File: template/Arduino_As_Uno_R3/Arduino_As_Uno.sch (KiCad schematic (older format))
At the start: 4 parts, among them P1 Power, P2 Analog, P3 Digital, P4 Digital

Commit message: correction holes
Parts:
- added P5, P6, P7, P8: CONN_1, Connect:1pin, symbol CONN_1
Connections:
- no-connect marks 1 -> 5
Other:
- note added: "Holes"
- moved on the sheet: P1, P2, P3, P4

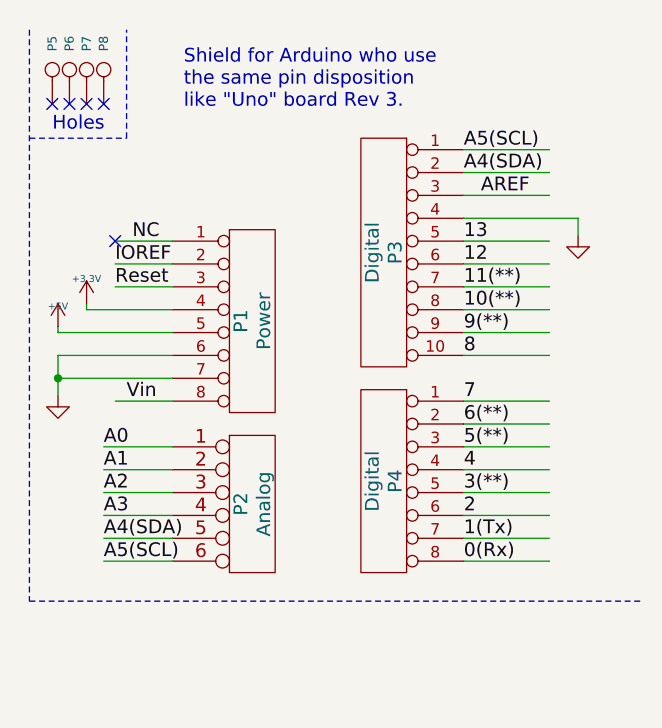
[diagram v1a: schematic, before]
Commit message: correct num holes and add Nano board
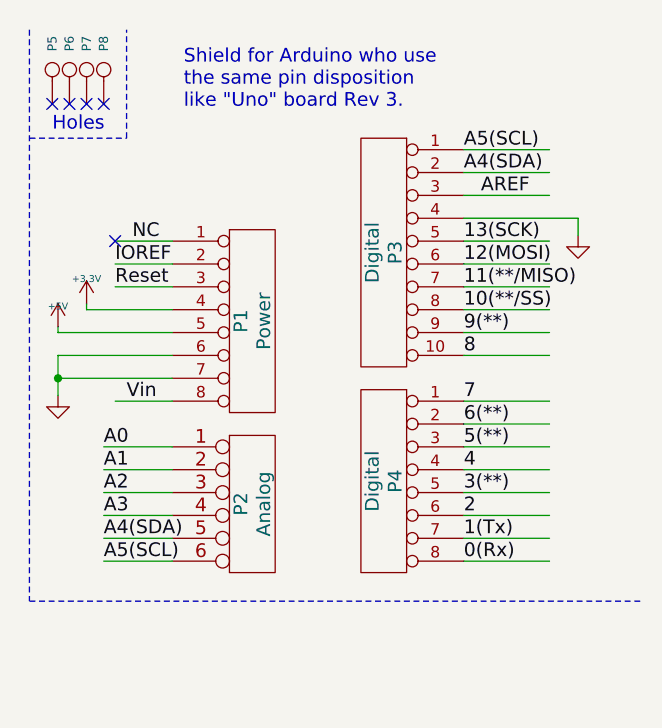
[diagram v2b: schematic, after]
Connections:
- net labels added: 10(**/SS), 11(**/MISO), 12(MOSI), 13(SCK)
- net labels removed: 10(**), 11(**), 12, 13
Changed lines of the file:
@@
 9(**)
 Text Label 10450 1700 0    60   ~ 0
-10(**)
+10(**/SS)
 Text Label 10450 1600 0    60   ~ 0
-11(**)
+11(**/MISO)
 Text Label 10450 1500 0    60   ~ 0
-12
+12(MOSI)
 Text Label 10450 1400 0    60   ~ 0
-13
+13(SCK)
 Text Label 10525 1200 0    60   ~ 0
 AREF

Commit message: Correction schématics
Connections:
- net labels added: 11(**/MOSI), 12(MISO)
- net labels removed: 11(**/MISO), 12(MOSI)
- wire segments 36 -> 38
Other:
- moved on the sheet: P1, P2, P3, P4, P5, P6, P7, P8

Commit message: corrections
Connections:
- net labels removed: NC
- wire segments 38 -> 37
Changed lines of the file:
@@
 	1    0    0    -1
 $EndComp
-NoConn ~ 8600 1525
-Text Label 8625 1525 0    60   ~ 0
-NC
+NoConn ~ 9375 1525
 Text Label 10550 1225 0    60   ~ 0
 A4(SDA)
@@
 	9300 2025 9300 3100
 Wire Wire Line
-	8600 1525 9375 1525
-Wire Wire Line
 	8600 1725 9375 1725

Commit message: add footprint Uno and Mega
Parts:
- P5, P6, P7, P8: footprint Connect:1pin -> Socket_Arduino_Uno:Arduino_1pin
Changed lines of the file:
@@
 F 0 "P5" H 10955 650 40  0000 L CNN
 F 1 "CONN_1" H 10875 705 30  0001 C CNN
-F 2 "Connect:1pin" H 10875 650 60  0001 C CNN
+F 2 "Socket_Arduino_Uno:Arduino_1pin" H 10875 650 60  0001 C CNN
 F 3 "" H 10875 650 60  0000 C CNN
 	1    10875 650
@@
 F 0 "P6" H 11030 650 40  0000 L CNN
 F 1 "CONN_1" H 10950 705 30  0001 C CNN
-F 2 "Connect:1pin" H 10950 650 60  0001 C CNN
+F 2 "Socket_Arduino_Uno:Arduino_1pin" H 10950 650 60  0001 C CNN
 F 3 "" H 10950 650 60  0000 C CNN
 	1    10950 650
@@
 F 0 "P7" H 11105 650 40  0000 L CNN
 F 1 "CONN_1" H 11025 705 30  0001 C CNN
-F 2 "Connect:1pin" H 11025 650 60  0001 C CNN
+F 2 "Socket_Arduino_Uno:Arduino_1pin" H 11025 650 60  0001 C CNN
 F 3 "" H 11025 650 60  0000 C CNN
 	1    11025 650
@@
 F 0 "P8" H 11180 650 40  0000 L CNN
 F 1 "CONN_1" H 11100 705 30  0001 C CNN
-F 2 "Connect:1pin" H 11100 650 60  0001 C CNN
+F 2 "Socket_Arduino_Uno:Arduino_1pin" H 11100 650 60  0001 C CNN
 F 3 "" H 11100 650 60  0000 C CNN
 	1    11100 650

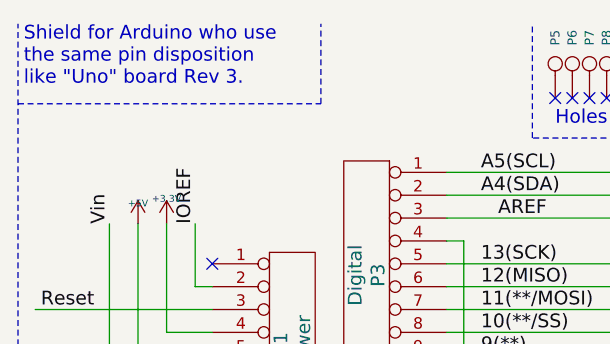
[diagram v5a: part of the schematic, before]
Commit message: correction text board Uno
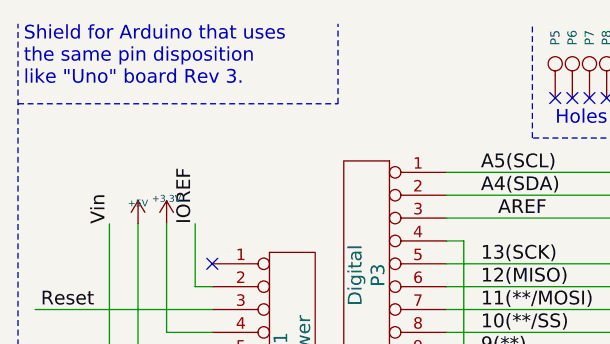
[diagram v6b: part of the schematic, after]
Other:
- note added: "Shield for Arduino that uses\nthe same pin disposition\nlike "Uno" board Rev 3."
- note removed: "Shield for Arduino who use \nthe same pin disposition \nlike "Uno" board Rev 3."
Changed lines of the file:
@@
 Text Label 10550 1125 0    60   ~ 0
 A5(SCL)
-Text Notes 8550 750  0    60   ~ 0
-Shield for Arduino who use \nthe same pin disposition \nlike "Uno" board Rev 3.
 $Comp
 L CONN_1 P5
@@
 	8525 3225 8525 475
 Wire Notes Line
-	8525 825  9850 825
+	8525 825  9925 825
+Text Notes 8550 750  0    60   ~ 0
+Shield for Arduino that uses\nthe same pin disposition\nlike "Uno" board Rev 3.
 Wire Notes Line
-	9850 825  9850 475
+	9925 825  9925 475
 $EndSCHEMATC

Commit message: rebuilt shematic and fix librairie
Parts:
- removed P1: Power, Socket_Arduino_Uno:Socket_Strip_Arduino_1x08, symbol CONN_8
- removed P2: Analog, Socket_Arduino_Uno:Socket_Strip_Arduino_1x06, symbol CONN_6
- removed P3: Digital, Socket_Arduino_Uno:Socket_Strip_Arduino_1x10, symbol CONN_10
- removed P4: Digital, Socket_Arduino_Uno:Socket_Strip_Arduino_1x08, symbol CONN_8
- removed P5, P6, P7, P8: CONN_1, Socket_Arduino_Uno:Arduino_1pin, symbol CONN_1
- added P1: Power, Socket_Arduino_Uno:Socket_Strip_Arduino_1x08, symbol CONN_01X08
- added P2: Analog, Socket_Arduino_Uno:Socket_Strip_Arduino_1x06, symbol CONN_01X06
- added P3: Digital, Socket_Arduino_Uno:Socket_Strip_Arduino_1x10, symbol CONN_01X10
- added P4: Digital, Socket_Arduino_Uno:Socket_Strip_Arduino_1x08, symbol CONN_01X08
- added P5, P6, P7, P8: CONN_01X01, Socket_Arduino_Uno:Arduino_1pin, symbol CONN_01X01
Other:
- note added: "1"

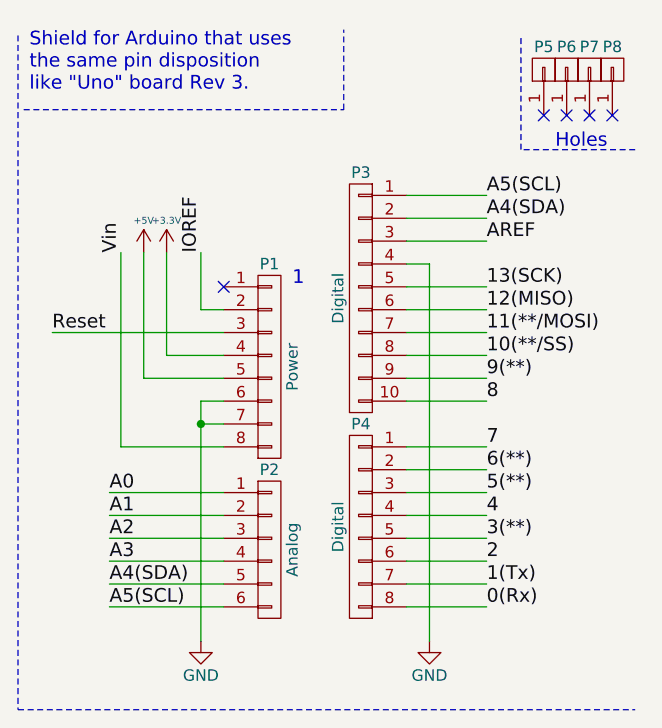
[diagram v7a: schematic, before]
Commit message: fix template
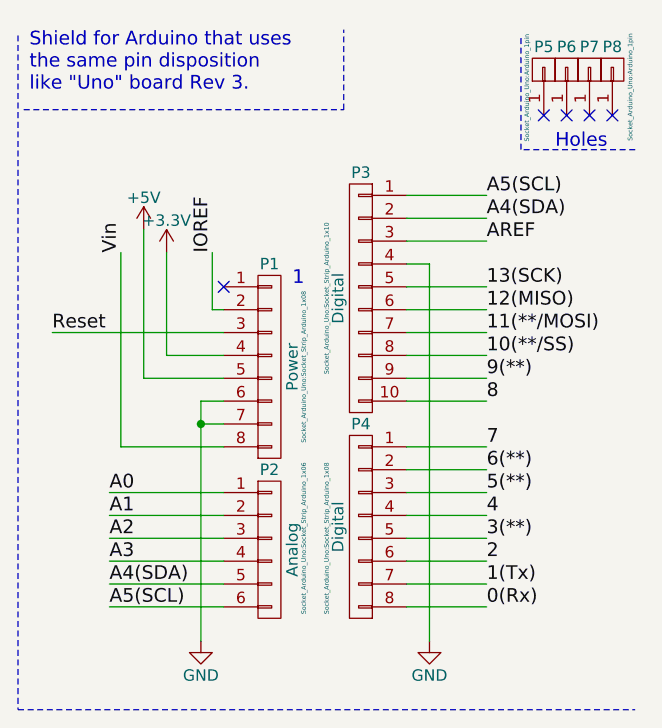
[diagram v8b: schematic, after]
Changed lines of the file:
@@
 Text Label 8950 1450 1    60   ~ 0
 Vin
-Text Label 9300 1450 1    60   ~ 0
+Text Label 9350 1450 1    60   ~ 0
 IOREF
 Text Label 8900 2500 0    60   ~ 0
@@
 F 0 "P1" H 9600 2400 50  0000 C CNN
 F 1 "Power" V 9700 1950 50  0000 C CNN
-F 2 "Socket_Arduino_Uno:Socket_Strip_Arduino_1x08" H 9600 1950 50  0001 C CNN
+F 2 "Socket_Arduino_Uno:Socket_Strip_Arduino_1x08" V 9750 1950 20  0000 C CNN
 F 3 "" H 9600 1950 50  0000 C CNN
 	1    9600 1950
@@
 P 9150 1450
 F 0 "#PWR01" H 9150 1300 50  0001 C CNN
-F 1 "+3.3V" H 9150 1590 30  0000 C CNN
+F 1 "+3.3V" H 9150 1590 50  0000 C CNN
 F 2 "" H 9150 1450 50  0000 C CNN
 F 3 "" H 9150 1450 50  0000 C CNN
@@
 L +5V #PWR02
 U 1 1 56D707BB
-P 9050 1450
-F 0 "#PWR02" H 9050 1300 50  0001 C CNN
-F 1 "+5V" H 9050 1590 30  0000 C CNN
-F 2 "" H 9050 1450 50  0000 C CNN
-F 3 "" H 9050 1450 50  0000 C CNN
-	1    9050 1450
+P 9050 1350
+F 0 "#PWR02" H 9050 1200 50  0001 C CNN
+F 1 "+5V" H 9050 1490 50  0000 C CNN
+F 2 "" H 9050 1350 50  0000 C CNN
+F 3 "" H 9050 1350 50  0000 C CNN
+	1    9050 1350
 	1    0    0    -1
 $EndComp
@@
 F 0 "P2" H 9600 3100 50  0000 C CNN
 F 1 "Analog" V 9700 2750 50  0000 C CNN
-F 2 "Socket_Arduino_Uno:Socket_Strip_Arduino_1x06" H 9600 2750 50  0001 C CNN
+F 2 "Socket_Arduino_Uno:Socket_Strip_Arduino_1x06" V 9750 2800 20  0000 C CNN
 F 3 "" H 9600 2750 50  0000 C CNN
 	1    9600 2750
@@
 F 0 "P5" V 10900 650 50  0000 C CNN
 F 1 "CONN_01X01" V 10900 650 50  0001 C CNN
-F 2 "Socket_Arduino_Uno:Arduino_1pin" H 10800 650 50  0001 C CNN
+F 2 "Socket_Arduino_Uno:Arduino_1pin" H 10721 724 20  0000 C CNN
 F 3 "" H 10800 650 50  0000 C CNN
 	1    10800 650
@@
 F 0 "P6" V 11000 650 50  0000 C CNN
 F 1 "CONN_01X01" V 11000 650 50  0001 C CNN
-F 2 "Socket_Arduino_Uno:Arduino_1pin" H 10900 650 50  0001 C CNN
+F 2 "Socket_Arduino_Uno:Arduino_1pin" H 10900 650 20  0001 C CNN
 F 3 "" H 10900 650 50  0000 C CNN
 	1    10900 650
@@
 F 0 "P7" V 11100 650 50  0000 C CNN
 F 1 "CONN_01X01" V 11100 650 50  0001 C CNN
-F 2 "Socket_Arduino_Uno:Arduino_1pin" H 11000 650 50  0001 C CNN
+F 2 "Socket_Arduino_Uno:Arduino_1pin" V 11000 650 20  0001 C CNN
 F 3 "" H 11000 650 50  0000 C CNN
 	1    11000 650
@@
 F 0 "P8" V 11200 650 50  0000 C CNN
 F 1 "CONN_01X01" V 11200 650 50  0001 C CNN
-F 2 "Socket_Arduino_Uno:Arduino_1pin" H 11100 650 50  0001 C CNN
+F 2 "Socket_Arduino_Uno:Arduino_1pin" H 11024 572 20  0000 C CNN
 F 3 "" H 11100 650 50  0000 C CNN
 	1    11100 650
@@
 F 0 "P4" H 10000 3100 50  0000 C CNN
 F 1 "Digital" V 10100 2650 50  0000 C CNN
-F 2 "Socket_Arduino_Uno:Socket_Strip_Arduino_1x08" H 10000 2650 50  0001 C CNN
+F 2 "Socket_Arduino_Uno:Socket_Strip_Arduino_1x08" V 10150 2600 20  0000 C CNN
 F 3 "" H 10000 2650 50  0000 C CNN
 	1    10000 2650
@@
 	9925 825  9925 475
 Wire Wire Line
-	9300 1450 9300 1700
-Wire Wire Line
-	9300 1700 9400 1700
+	9350 1450 9350 1700
+Wire Wire Line
+	9350 1700 9400 1700
 Wire Wire Line
 	9400 1900 9150 1900
@@
 	8950 2300 8950 1450
 Wire Wire Line
-	9050 2000 9050 1450
+	9050 2000 9050 1350
 Wire Wire Line
 	9150 1900 9150 1450
@@
 F 0 "P3" H 10000 2200 50  0000 C CNN
 F 1 "Digital" V 10100 1650 50  0000 C CNN
-F 2 "Socket_Arduino_Uno:Socket_Strip_Arduino_1x10" H 10000 1650 50  0001 C CNN
+F 2 "Socket_Arduino_Uno:Socket_Strip_Arduino_1x10" V 10150 1650 20  0000 C CNN
 F 3 "" H 10000 1650 50  0000 C CNN
 	1    10000 1650
@@
 	10300 1500 10300 3150
 Wire Wire Line
-	9300 2100 9300 3150
+	9300 2100 9300 2200
+Wire Wire Line
+	9300 2200 9300 3150
 Wire Notes Line
 	8500 500  8500 3450
